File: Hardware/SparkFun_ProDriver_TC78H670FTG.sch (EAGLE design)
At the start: 42 parts, among them J1 POWER_JACKTOE, J2 LATCH, J3 PTH, J4 LATCH, J5 LATCH, J6 PTH, J7 LATCH, J8 PTH, U1 TC78H670FTG

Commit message: moved connectors inward to allow for depanel blade space
Also added tcream to IC package
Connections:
- net N$3 renamed RAW
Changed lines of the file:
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@@
 <grid distance="0.1" unitdist="inch" unit="inch" style="lines" multiple="1" display="no" altdistance="0.01" altunitdist="inch" altunit="inch"/>
 <layers>
-<layer number="1" name="Top" color="4" fill="1" visible="yes" active="no"/>
-<layer number="2" name="Route2" color="14" fill="1" visible="yes" active="no"/>
-<layer number="3" name="Route3" color="4" fill="3" visible="yes" active="no"/>
-<layer number="4" name="Route4" color="1" fill="4" visible="yes" active="no"/>
-<layer number="5" name="Route5" color="4" fill="4" visible="yes" active="no"/>
-<layer number="6" name="Route6" color="1" fill="8" visible="yes" active="no"/>
-<layer number="7" name="Route7" color="4" fill="8" visible="yes" active="no"/>
-<layer number="8" name="Route8" color="1" fill="2" visible="yes" active="no"/>
-<layer number="9" name="Route9" color="4" fill="2" visible="yes" active="no"/>
-<layer number="10" name="Route10" color="1" fill="7" visible="yes" active="no"/>
-<layer number="11" name="Route11" color="4" fill="7" visible="yes" active="no"/>
-<layer number="12" name="Route12" color="1" fill="5" visible="yes" active="no"/>
-<layer number="13" name="Route13" color="4" fill="5" visible="yes" active="no"/>
-<layer number="14" name="Route14" color="1" fill="6" visible="yes" active="no"/>
-<layer number="15" name="Route15" color="13" fill="1" visible="yes" active="no"/>
-<layer number="16" name="Bottom" color="1" fill="1" visible="yes" active="no"/>
-<layer number="17" name="Pads" color="2" fill="1" visible="yes" active="no"/>
-<layer number="18" name="Vias" color="2" fill="1" visible="yes" active="no"/>
-<layer number="19" name="Unrouted" color="6" fill="1" visible="yes" active="no"/>
-<layer number="20" name="Dimension" color="24" fill="1" visible="yes" active="no"/>
-<layer number="21" name="tPlace" color="16" fill="1" visible="yes" active="no"/>
-<layer number="22" name="bPlace" color="14" fill="1" visible="yes" active="no"/>
-<layer number="23" name="tOrigins" color="15" fill="1" visible="yes" active="no"/>
-<layer number="24" name="bOrigins" color="15" fill="1" visible="yes" active="no"/>
-<layer number="25" name="tNames" color="7" fill="1" visible="yes" active="no"/>
-<layer number="26" name="bNames" color="7" fill="1" visible="yes" active="no"/>
-<layer number="27" name="tValues" color="7" fill="1" visible="yes" active="no"/>
-<layer number="28" name="bValues" color="7" fill="1" visible="yes" active="no"/>
+<layer number="1" name="Top" color="4" fill="1" visible="no" active="no"/>
+<layer number="2" name="Route2" color="14" fill="1" visible="no" active="no"/>
+<layer number="3" name="Route3" color="4" fill="3" visible="no" active="no"/>
+<layer number="4" name="Route4" color="1" fill="4" visible="no" active="no"/>
+<layer number="5" name="Route5" color="4" fill="4" visible="no" active="no"/>
+<layer number="6" name="Route6" color="1" fill="8" visible="no" active="no"/>
+<layer number="7" name="Route7" color="4" fill="8" visible="no" active="no"/>
+<layer number="8" name="Route8" color="1" fill="2" visible="no" active="no"/>
+<layer number="9" name="Route9" color="4" fill="2" visible="no" active="no"/>
+<layer number="10" name="Route10" color="1" fill="7" visible="no" active="no"/>
+<layer number="11" name="Route11" color="4" fill="7" visible="no" active="no"/>
+<layer number="12" name="Route12" color="1" fill="5" visible="no" active="no"/>
+<layer number="13" name="Route13" color="4" fill="5" visible="no" active="no"/>
+<layer number="14" name="Route14" color="1" fill="6" visible="no" active="no"/>
+<layer number="15" name="Route15" color="13" fill="1" visible="no" active="no"/>
+<layer number="16" name="Bottom" color="1" fill="1" visible="no" active="no"/>
+<layer number="17" name="Pads" color="2" fill="1" visible="no" active="no"/>
+<layer number="18" name="Vias" color="2" fill="1" visible="no" active="no"/>
+<layer number="19" name="Unrouted" color="6" fill="1" visible="no" active="no"/>
+<layer number="20" name="Dimension" color="24" fill="1" visible="no" active="no"/>
+<layer number="21" name="tPlace" color="16" fill="1" visible="no" active="no"/>
+<layer number="22" name="bPlace" color="14" fill="1" visible="no" active="no"/>
+<layer number="23" name="tOrigins" color="15" fill="1" visible="no" active="no"/>
+<layer number="24" name="bOrigins" color="15" fill="1" visible="no" active="no"/>
+<layer number="25" name="tNames" color="7" fill="1" visible="no" active="no"/>
+<layer number="26" name="bNames" color="7" fill="1" visible="no" active="no"/>
+<layer number="27" name="tValues" color="7" fill="1" visible="no" active="no"/>
+<layer number="28" name="bValues" color="7" fill="1" visible="no" active="no"/>
 <layer number="29" name="tStop" color="30" fill="5" visible="no" active="no"/>
 <layer number="30" name="bStop" color="7" fill="6" visible="no" active="no"/>
@@
 <layer number="35" name="tGlue" color="7" fill="4" visible="no" active="no"/>
 <layer number="36" name="bGlue" color="7" fill="5" visible="no" active="no"/>
-<layer number="37" name="tTest" color="7" fill="1" visible="yes" active="no"/>
-<layer number="38" name="bTest" color="7" fill="1" visible="yes" active="no"/>
+<layer number="37" name="tTest" color="7" fill="1" visible="no" active="no"/>
+<layer number="38" name="bTest" color="7" fill="1" visible="no" active="no"/>
 <layer number="39" name="tKeepout" color="4" fill="11" visible="no" active="no"/>
 <layer number="40" name="bKeepout" color="1" fill="11" visible="no" active="no"/>
@@
 <layer number="44" name="Drills" color="7" fill="1" visible="no" active="no"/>
 <layer number="45" name="Holes" color="7" fill="1" visible="no" active="no"/>
-<layer number="46" name="Milling" color="3" fill="1" visible="yes" active="no"/>
-<layer number="47" name="Measures" color="7" fill="1" visible="yes" active="no"/>
-<layer number="48" name="Document" color="7" fill="1" visible="yes" active="no"/>
-<layer number="49" name="Reference" color="7" fill="1" visible="yes" active="no"/>
-<layer number="50" name="dxf" color="7" fill="1" visible="yes" active="no"/>
-<layer number="51" name="tDocu" color="6" fill="1" visible="yes" active="no"/>
-<layer number="52" name="bDocu" color="7" fill="1" visible="yes" active="no"/>
-<layer number="53" name="tGND_GNDA" color="7" fill="9" visible="yes" active="no"/>
-<layer number="54" name="bGND_GNDA" color="1" fill="9" visible="yes" active="no"/>
-<layer number="56" name="wert" color="7" fill="1" visible="yes" active="no"/>
-<layer number="57" name="tCAD" color="7" fill="1" visible="yes" active="no"/>
-<layer number="59" name="tCarbon" color="7" fill="1" visible="yes" active="no"/>
-<layer number="60" name="bCarbon" color="7" fill="1" visible="yes" active="no"/>
+<layer number="46" name="Milling" color="3" fill="1" visible="no" active="no"/>
+<layer number="47" name="Measures" color="7" fill="1" visible="no" active="no"/>
+<layer number="48" name="Document" color="7" fill="1" visible="no" active="no"/>
+<layer number="49" name="Reference" color="7" fill="1" visible="no" active="no"/>
+<layer number="50" name="dxf" color="7" fill="1" visible="no" active="no"/>
+<layer number="51" name="tDocu" color="6" fill="1" visible="no" active="no"/>
+<layer number="52" name="bDocu" color="7" fill="1" visible="no" active="no"/>
+<layer number="53" name="tGND_GNDA" color="7" fill="9" visible="no" active="no"/>
+<layer number="54" name="bGND_GNDA" color="1" fill="9" visible="no" active="no"/>
+<layer number="56" name="wert" color="7" fill="1" visible="no" active="no"/>
+<layer number="57" name="tCAD" color="7" fill="1" visible="no" active="no"/>
+<layer number="59" name="tCarbon" color="7" fill="1" visible="no" active="no"/>
+<layer number="60" name="bCarbon" color="7" fill="1" visible="no" active="no"/>
 <layer number="88" name="SimResults" color="9" fill="1" visible="yes" active="yes"/>
 <layer number="89" name="SimProbes" color="9" fill="1" visible="yes" active="yes"/>
@@
 </segment>
 </net>
-<net name="N$3" class="0">
+<net name="RAW" class="0">
 <segment>
 <pinref part="J3" gate="G$1" pin="2"/>

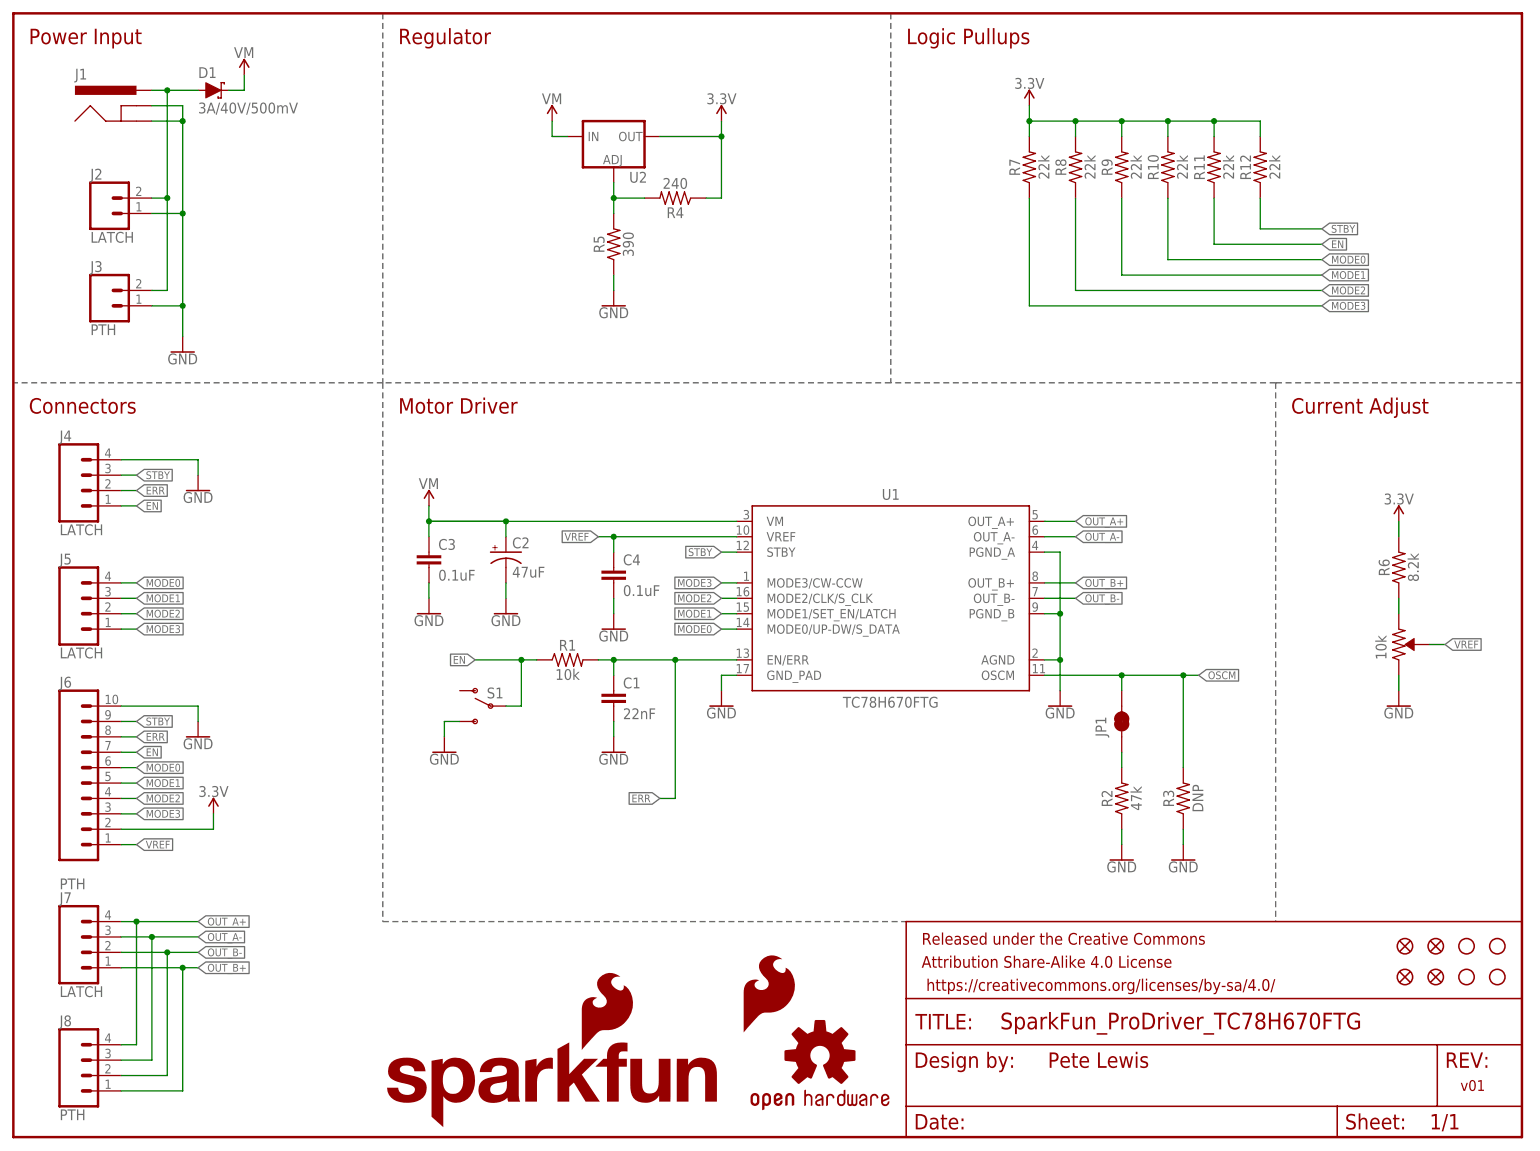
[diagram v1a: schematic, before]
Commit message: Added PTC and 0Ohm res to power input
plus bypass jumpers down below
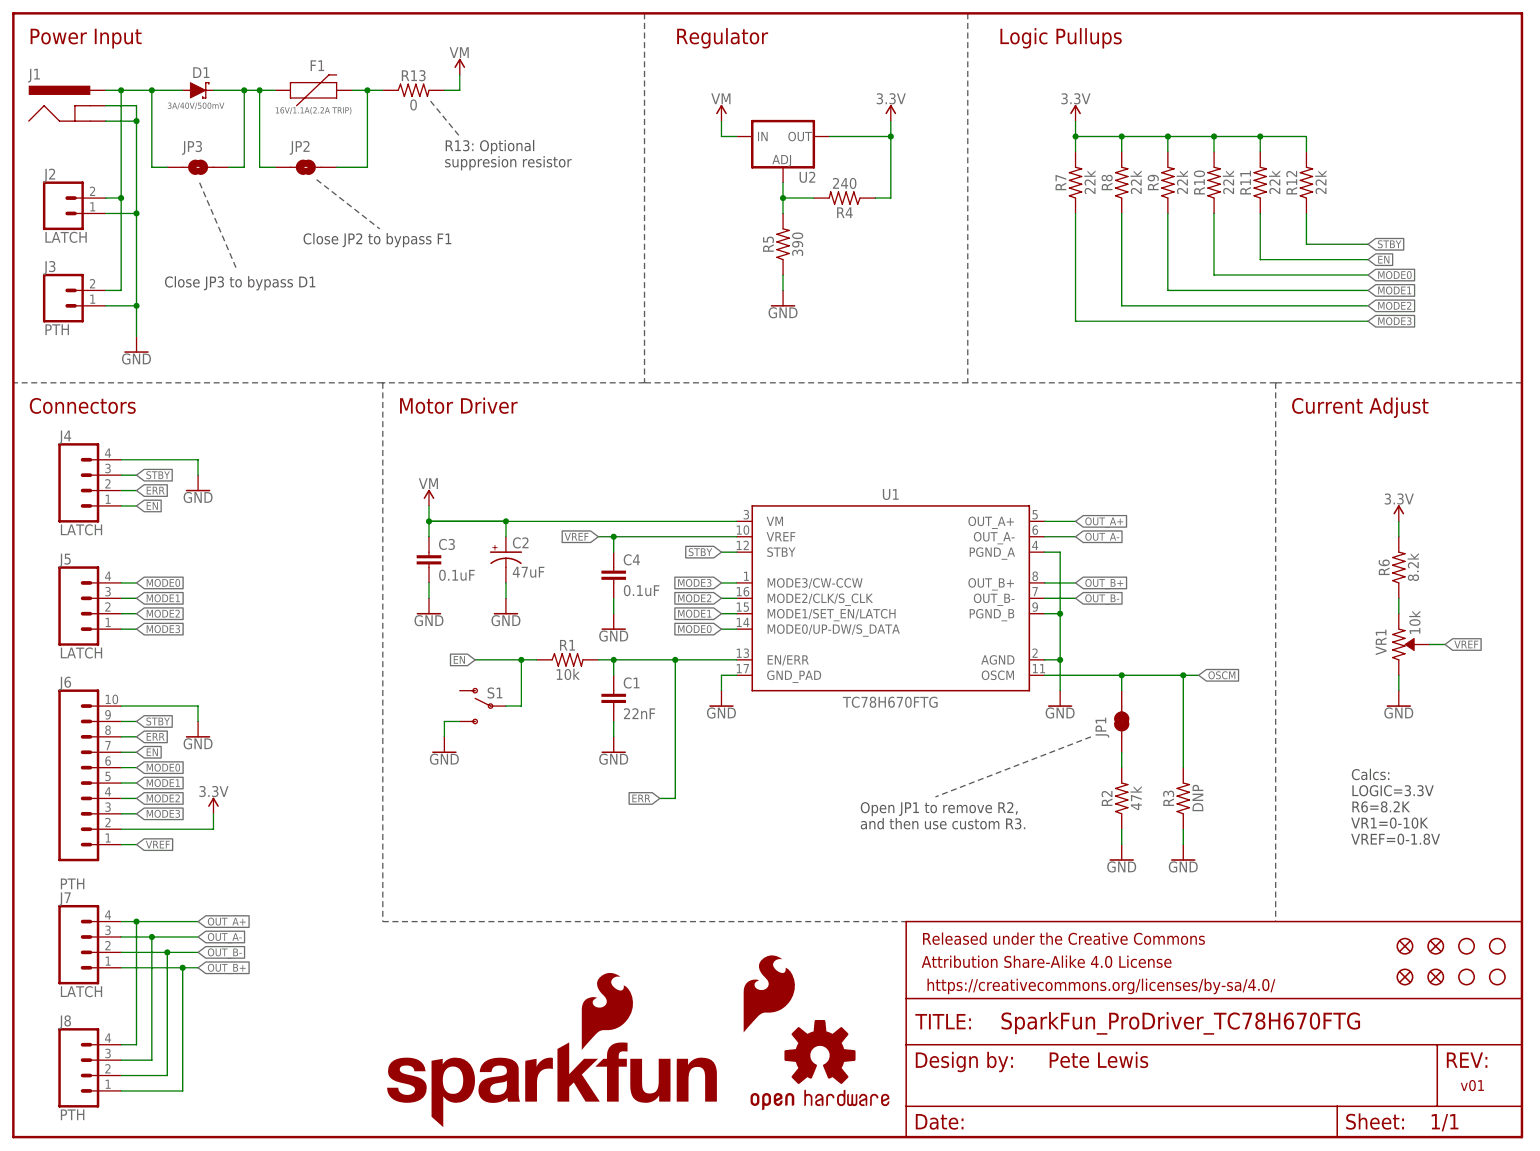
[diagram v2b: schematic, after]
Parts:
- added F1: 16V/1.1A(2.2A TRIP), TC78H670FTG:PPTC_16V_1.1A_(2.2ATRIP)
- added JP2, JP3: JUMPER-SMT_2_NO_SILK, SparkFun-Jumpers:JUMPER-SMT_2_NO_SILK
- added R13: 0, SparkFun-Resistors:0OHM-0603-1/10W-5%
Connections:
- new net N$1: D1.C, F1.1, JP2.1, JP3.2
- new net N$3: F1.2, JP2.2, R13.1
- net RAW: now also JP3.1
- net VM: now also R13.2; no longer D1.C
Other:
- note added: "Calcs: LOGIC=3.3V R6=8.2K VR1=0-10K VREF=0-1.8V"
- note added: "Close JP2 to bypass F1"
- note added: "Close JP3 to bypass D1"
- note added: "Open JP1 to remove R2, and then use custom R3."
- note added: "R13: Optional suppresion resistor"
- moved on the sheet: D1, J1, J2, J3, R10, R11, R12, R4, R5, R7, R8, R9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

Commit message: added value to lm1117 so it's visible in sch
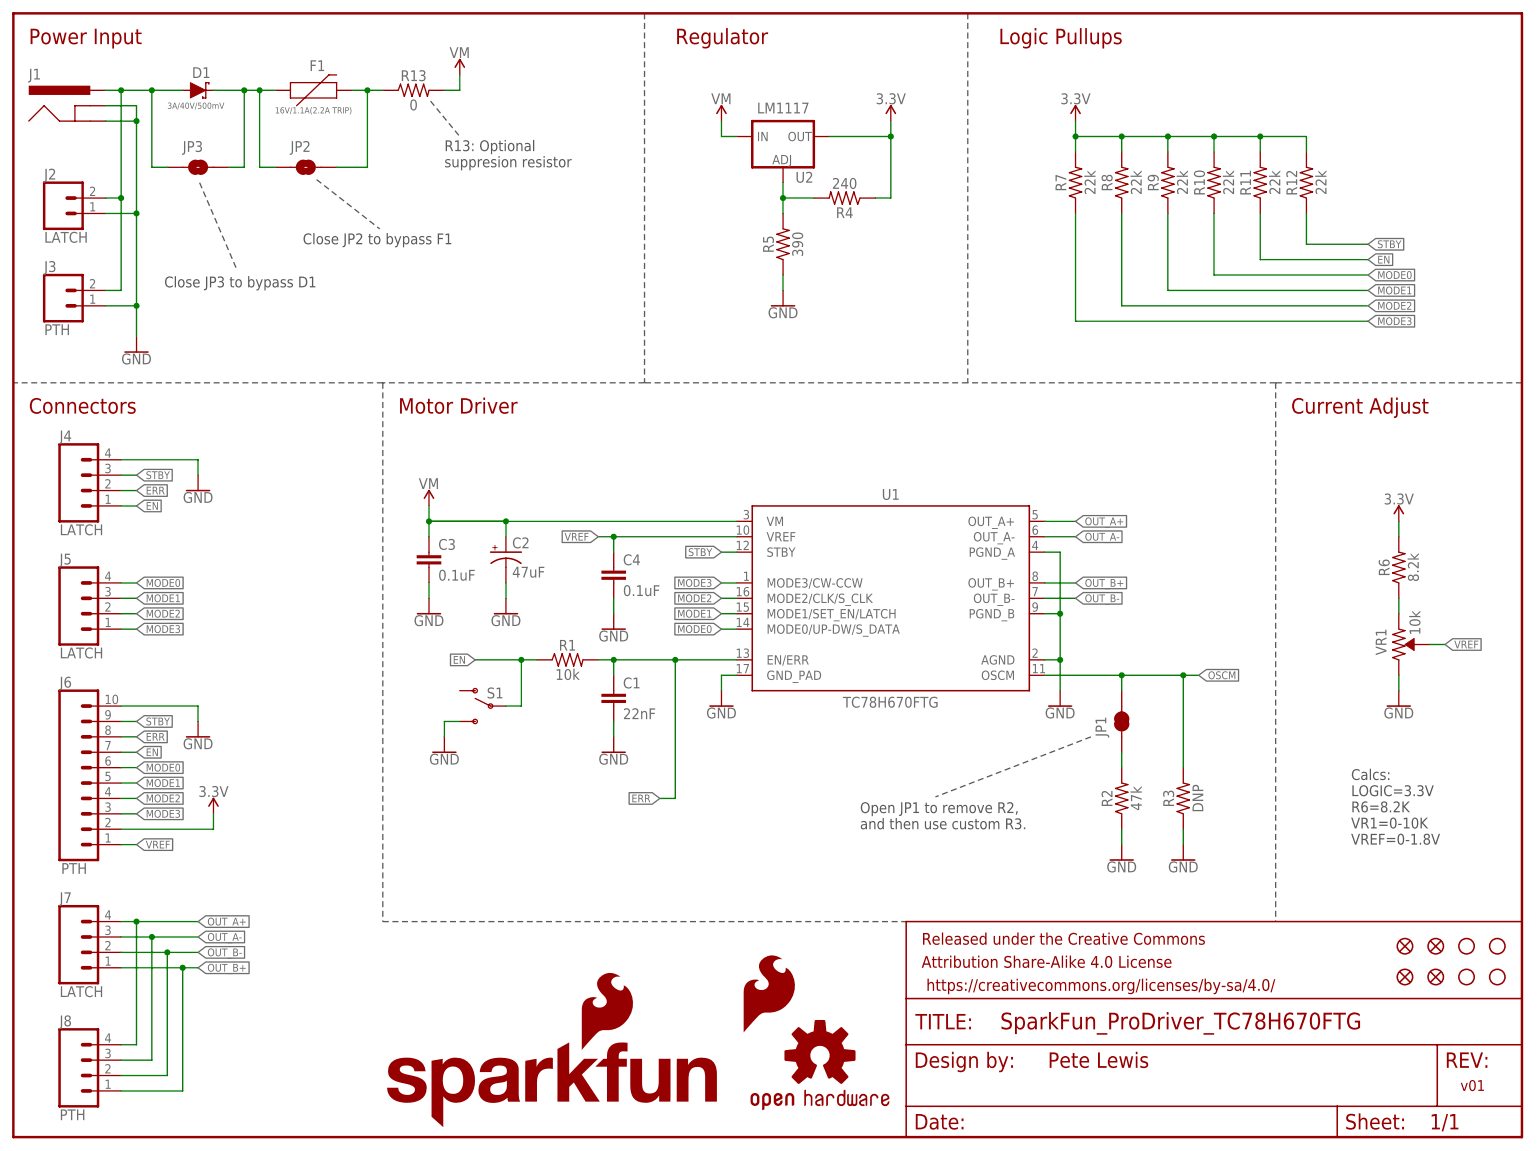
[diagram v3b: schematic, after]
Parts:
- U2: value (none) -> LM1117
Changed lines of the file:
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@@
 <part name="D1" library="SparkFun-DiscreteSemi" deviceset="DIODE-SCHOTTKY" device="-B340A" value="3A/40V/500mV"/>
 <part name="SUPPLY3" library="SparkFun-PowerSymbols" deviceset="VCC" device="" value="VM"/>
-<part name="U2" library="SparkFun-IC-Power" deviceset="V_REG_LM1117" device="SOT223"/>
+<part name="U2" library="SparkFun-IC-Power" deviceset="V_REG_LM1117" device="SOT223" value="LM1117"/>
 <part name="SUPPLY1" library="SparkFun-PowerSymbols" deviceset="VCC" device="" value="VM"/>
 <part name="R4" library="SparkFun-Resistors" deviceset="240OHM" device="-0603-1/10W-1%" value="240"/>
@@
 </instance>
 <instance part="U2" gate="G$1" x="127" y="165.1" smashed="yes">
-<attribute name="NAME" x="129.54" y="157.48" size="1.778" layer="95" font="vector"/>
-<attribute name="VALUE" x="129.54" y="154.94" size="1.778" layer="96"/>
+<attribute name="NAME" x="129.032" y="157.48" size="1.778" layer="95" font="vector"/>
+<attribute name="VALUE" x="122.682" y="168.91" size="1.778" layer="96" font="vector"/>
 </instance>
 <instance part="SUPPLY1" gate="G$1" x="116.84" y="167.64" smashed="yes">
@@
 </instance>
 <instance part="J6" gate="J1" x="7.62" y="66.04" smashed="yes">
-<attribute name="VALUE" x="7.62" y="40.894" size="1.778" layer="96" font="vector"/>
+<attribute name="VALUE" x="7.874" y="43.434" size="1.778" layer="96" font="vector"/>
 <attribute name="NAME" x="7.62" y="74.168" size="1.778" layer="95" font="vector"/>
 </instance>
